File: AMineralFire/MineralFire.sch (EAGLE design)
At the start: 49 parts, among them IC1 LM358, Q1 20MHz, T1 200mA/40V, U1 328P, U3 7805

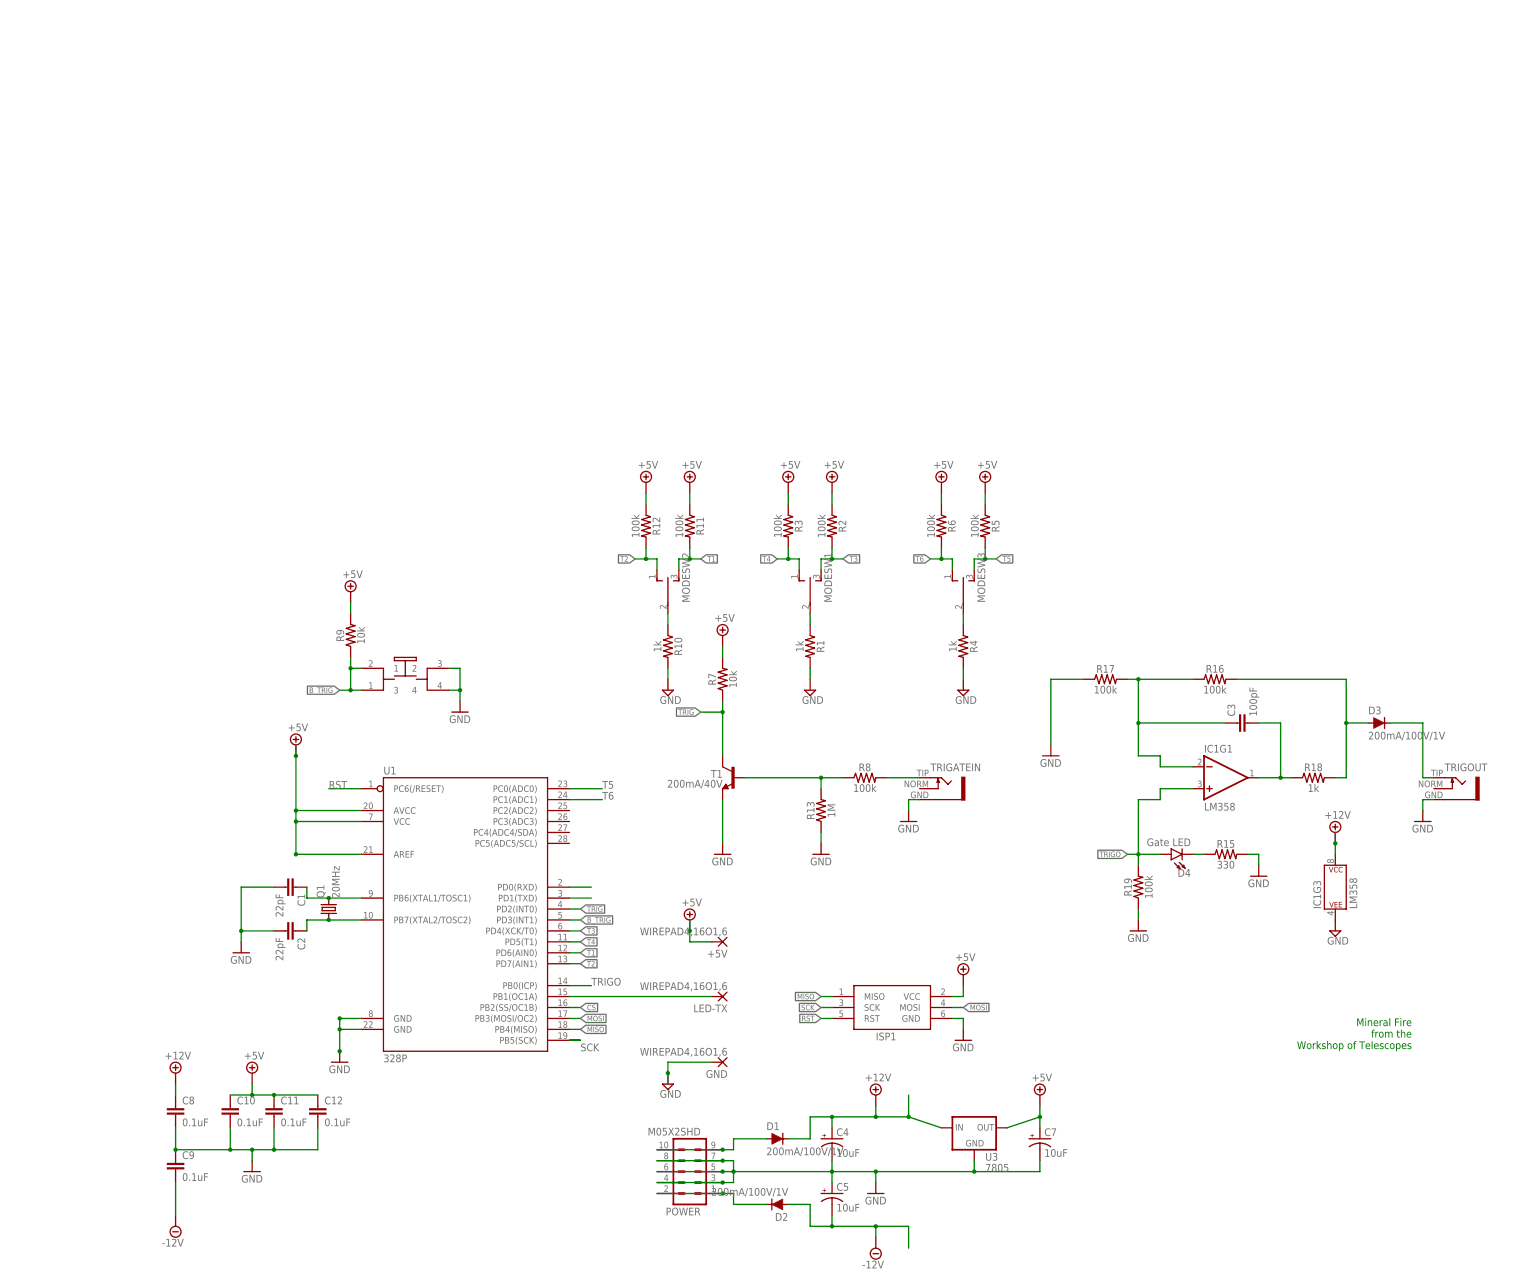
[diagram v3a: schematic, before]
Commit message: added LED in switch
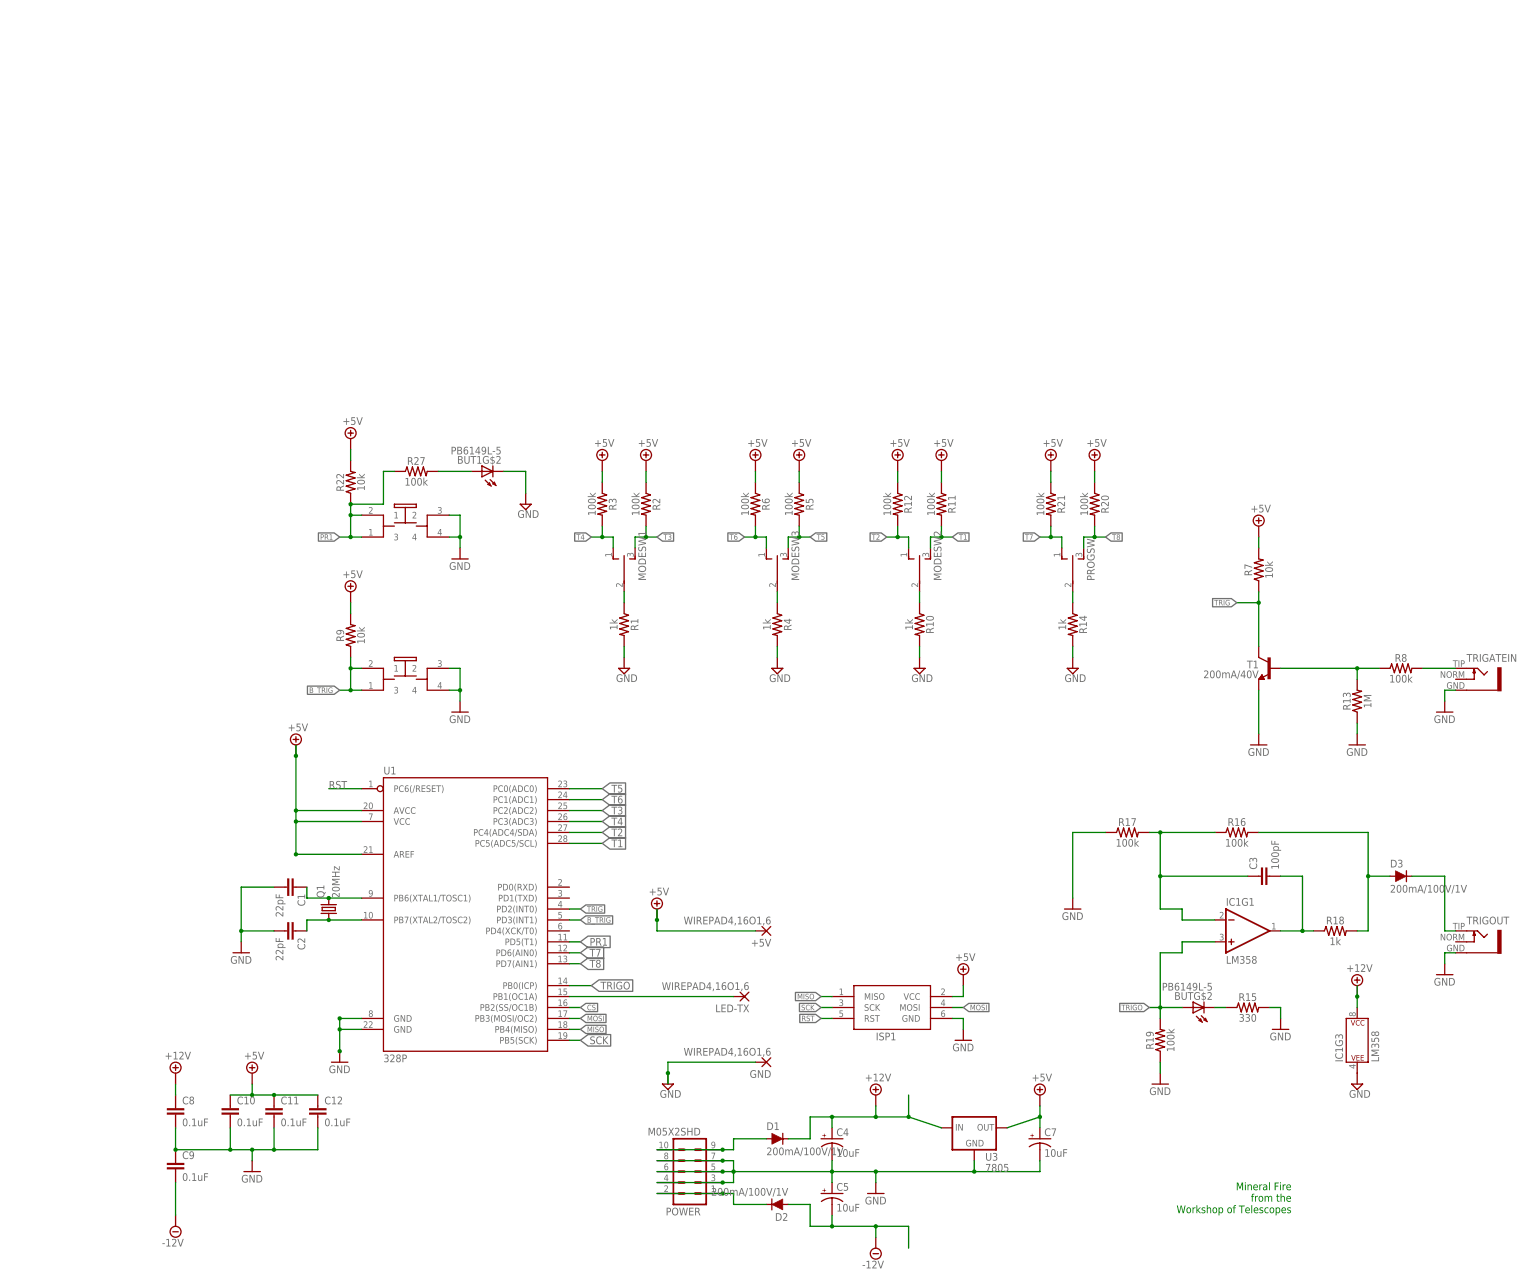
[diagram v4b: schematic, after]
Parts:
- removed D4: Gate LED, SparkFun-LED:LED3MM
- added BUT1: PB6149L-5, INSTRUO:PB6149L-5
- added PROGSW: TOGGLE_ON_OFF_ON, INSTRUO:TOGGLE_ON_OFF_ON
- added R14: 1k, SparkFun-Resistors:1KOHM-HORIZ-1/4W-5%
- added R20, R21, R27: 100k, SparkFun-Resistors:100KOHM-HORIZ-1/4W-5%
- added R22: 10k, SparkFun-Resistors:10KOHM-HORIZ-1/4W-1%
- renumbered START to BUT
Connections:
- new net N$16: BUT1G$2.A, R27.2
- new net N$6: PROGSW.P, R14.1
- new net PR1: BUT1G$1.1, BUT1G$1.3, R22.1, R27.1, U1.PD5(T1)
- new net T7: PROGSW.O, R21.2, U1.PD6(AIN0)
- new net T8: PROGSW.S, R20.2, U1.PD7(AIN1)
- net +5V: now also R20.1, R21.1, R22.2
- net GND: now also BUT1G$1.2, BUT1G$1.4, BUT1G$2.C, R14.2
- net N$31: now also BUTG$2.C; no longer D4.C
- net T1: now also U1.PC5(ADC5/SCL); no longer U1.PD6(AIN0)
- net T2: now also U1.PC4(ADC4/SDA); no longer U1.PD7(AIN1)
- net T3: now also U1.PC2(ADC2); no longer U1.PD4(XCK/T0)
- net T4: now also U1.PC3(ADC3); no longer U1.PD5(T1)
- net T5: no longer U1.PD0(RXD)
- net T6: no longer U1.PD1(TXD)
- net TRIGO: now also BUTG$2.A; no longer D4.A
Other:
- moved on the sheet: +5V, C3, D3, GND, IC1G1, IC1G3, LED-TX, MODESW1, MODESW2, MODESW3, R1, R10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

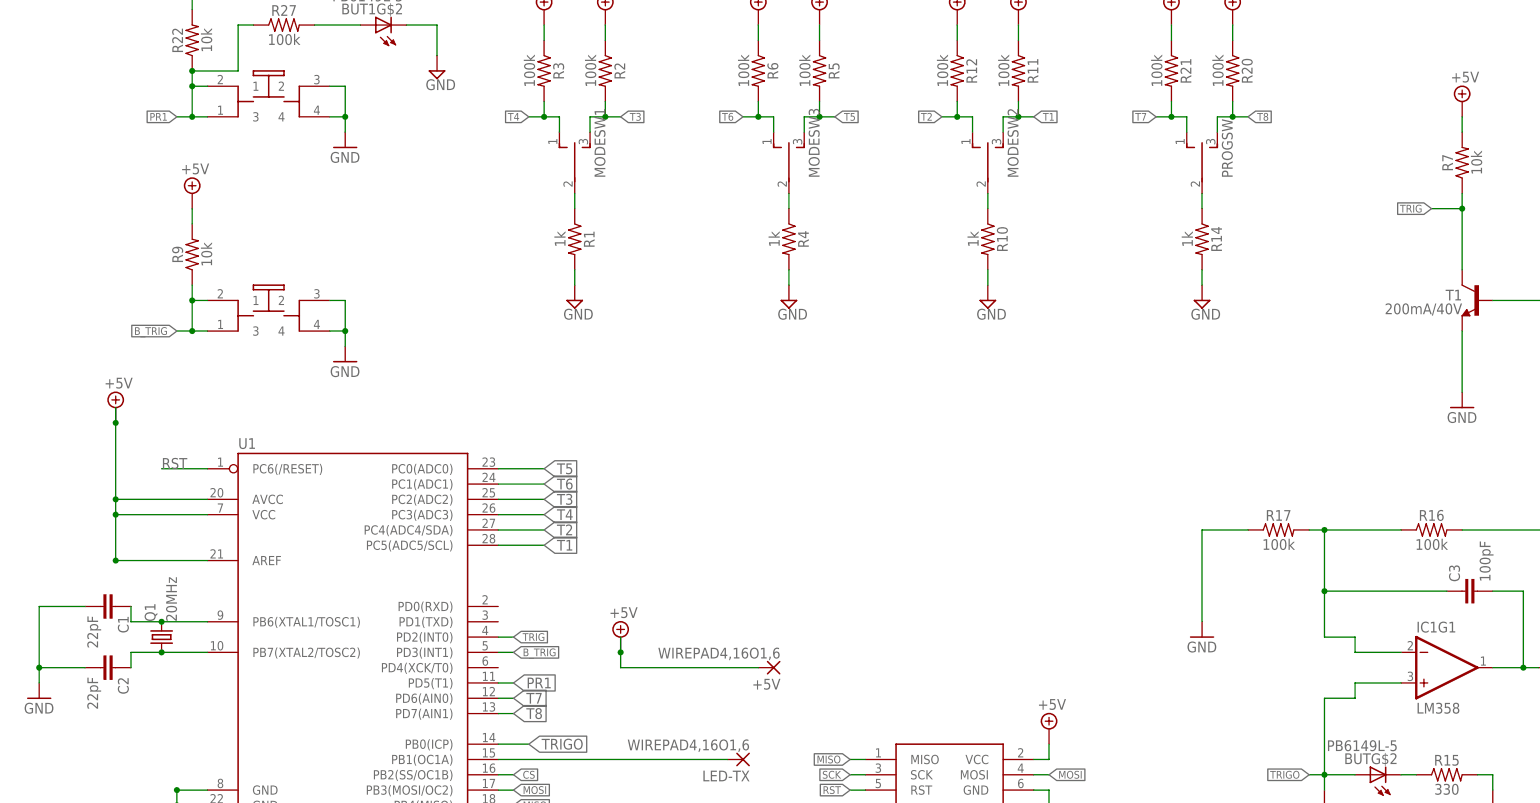
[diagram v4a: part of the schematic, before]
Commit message: Added AND gate on trigger
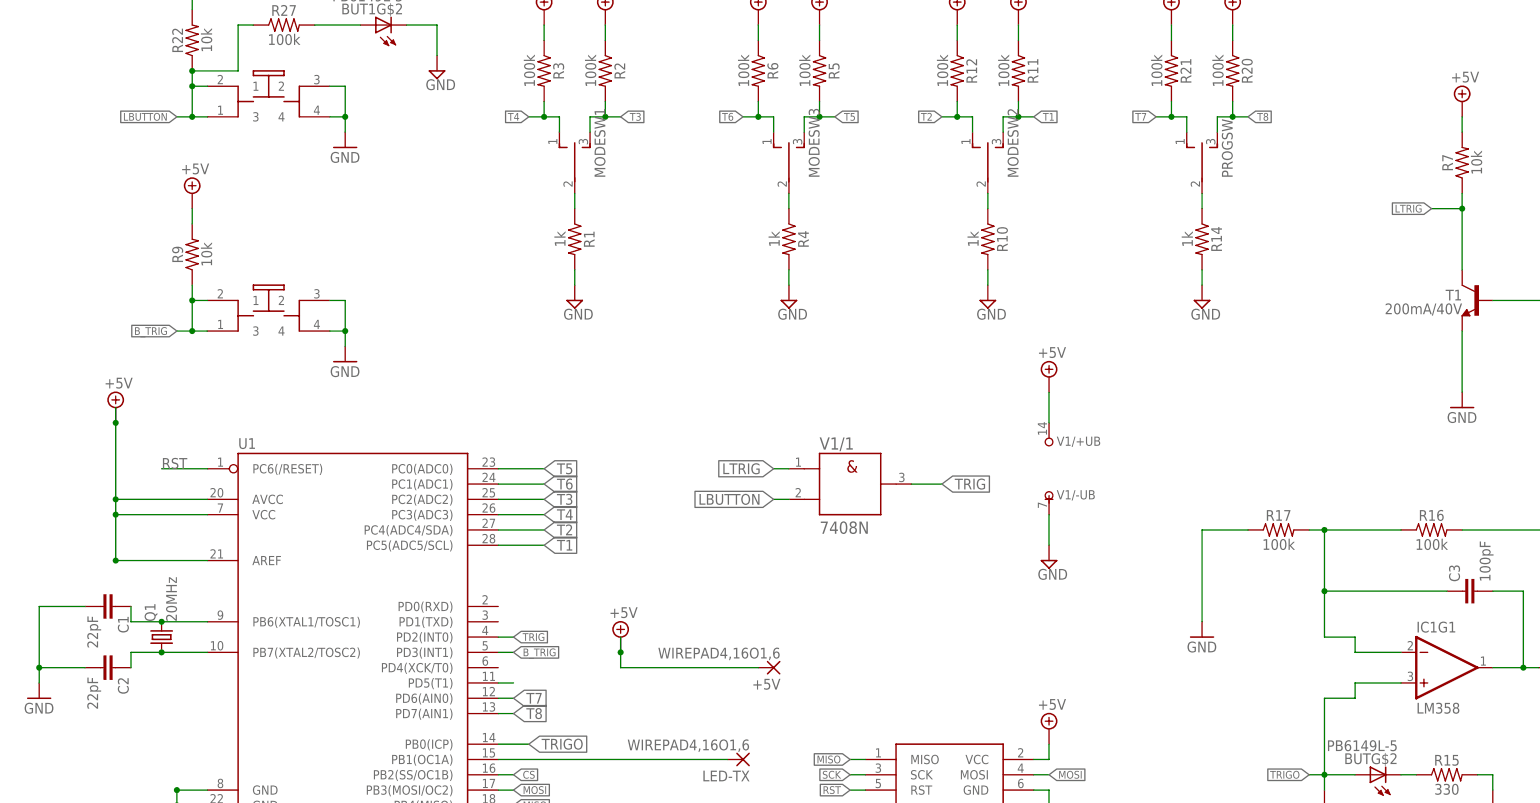
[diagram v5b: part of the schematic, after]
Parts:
- added V1: 7408N, 74ttl-din:7408N
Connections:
- new net LBUTTON: BUT1G$1.1, BUT1G$1.3, R22.1, R27.1, V1/1.B
- new net LTRIG: R7.1, T1.C, V1/1.A
- net +5V: now also V1/+UB.+UB
- net GND: now also V1/-UB.-UB
- net PR1: no longer BUT1G$1.1, BUT1G$1.3, R22.1, R27.1
- net TRIG: now also V1/1.Y; no longer R7.1, T1.C
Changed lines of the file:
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@@
 <part name="R27" library="SparkFun-Resistors" deviceset="100KOHM" device="-HORIZ-1/4W-5%" value="100k"/>
 <part name="SUPPLY30" library="supply2" deviceset="GND" device=""/>
+<part name="V1" library="74ttl-din" deviceset="74*08" device="N"/>
+<part name="SUPPLY28" library="supply2" deviceset="+5V" device=""/>
+<part name="SUPPLY29" library="supply2" deviceset="GND" device=""/>
 </parts>
 <sheets>
@@
 <instance part="R27" gate="G$1" x="76.2" y="142.24"/>
 <instance part="SUPPLY30" gate="GND" x="101.6" y="134.62"/>
+<instance part="V1" gate="/1" x="170.18" y="66.04"/>
+<instance part="V1" gate="/+UB" x="203.2" y="73.66"/>
+<instance part="SUPPLY28" gate="+5V" x="203.2" y="83.82"/>
+<instance part="V1" gate="/-UB" x="203.2" y="63.5"/>
+<instance part="SUPPLY29" gate="GND" x="203.2" y="53.34"/>
 </instances>
 <busses>
@@
 <pinref part="SUPPLY30" gate="GND" pin="GND"/>
 </segment>
+<segment>
+<pinref part="V1" gate="/-UB" pin="-UB"/>
+<wire x1="203.2" y1="60.96" x2="203.2" y2="55.88" width="0.1524" layer="91"/>
+<pinref part="SUPPLY29" gate="GND" pin="GND"/>
+</segment>
 </net>
 <net name="RST" class="0">
@@
 <pinref part="SUPPLY27" gate="+5V" pin="+5V"/>
 <wire x1="60.96" y1="147.32" x2="60.96" y2="144.78" width="0.1524" layer="91"/>
+</segment>
+<segment>
+<pinref part="V1" gate="/+UB" pin="+UB"/>
+<wire x1="203.2" y1="76.2" x2="203.2" y2="81.28" width="0.1524" layer="91"/>
+<pinref part="SUPPLY28" gate="+5V" pin="+5V"/>
 </segment>
 </net>
@@
 </segment>
 <segment>
-<pinref part="T1" gate="G$1" pin="C"/>
-<pinref part="R7" gate="G$1" pin="1"/>
-<wire x1="271.78" y1="114.3" x2="271.78" y2="111.76" width="0.1524" layer="91"/>
-<wire x1="271.78" y1="111.76" x2="271.78" y2="101.6" width="0.1524" layer="91"/>
-<wire x1="271.78" y1="111.76" x2="266.7" y2="111.76" width="0.1524" layer="91"/>
-<junction x="271.78" y="111.76"/>
-<label x="266.7" y="111.76" size="1.27" layer="95" rot="R180" xref="yes"/>
+<pinref part="V1" gate="/1" pin="Y"/>
+<wire x1="180.34" y1="66.04" x2="185.42" y2="66.04" width="0.1524" layer="91"/>
+<label x="185.42" y="66.04" size="1.778" layer="95" xref="yes"/>
 </segment>
 </net>
@@
 <pinref part="U1" gate="G$1" pin="PD5(T1)"/>
 <wire x1="111.76" y1="33.02" x2="114.3" y2="33.02" width="0.1524" layer="91"/>
-<label x="114.3" y="33.02" size="1.778" layer="95" xref="yes"/>
+</segment>
+</net>
+<net name="N$16" class="0">
+<segment>
+<pinref part="R27" gate="G$1" pin="2"/>
+<pinref part="BUT1" gate="G$2" pin="A"/>
+<wire x1="81.28" y1="142.24" x2="88.9" y2="142.24" width="0.1524" layer="91"/>
+</segment>
+</net>
+<net name="LTRIG" class="0">
+<segment>
+<pinref part="V1" gate="/1" pin="A"/>
+<wire x1="160.02" y1="68.58" x2="157.48" y2="68.58" width="0.1524" layer="91"/>
+<label x="157.48" y="68.58" size="1.778" layer="95" rot="R180" xref="yes"/>
+</segment>
+<segment>
+<pinref part="T1" gate="G$1" pin="C"/>
+<pinref part="R7" gate="G$1" pin="1"/>
+<wire x1="271.78" y1="114.3" x2="271.78" y2="111.76" width="0.1524" layer="91"/>
+<wire x1="271.78" y1="111.76" x2="271.78" y2="101.6" width="0.1524" layer="91"/>
+<wire x1="271.78" y1="111.76" x2="266.7" y2="111.76" width="0.1524" layer="91"/>
+<junction x="271.78" y="111.76"/>
+<label x="266.7" y="111.76" size="1.27" layer="95" rot="R180" xref="yes"/>
+</segment>
+</net>
+<net name="LBUTTON" class="0">
+<segment>
+<pinref part="V1" gate="/1" pin="B"/>
+<wire x1="160.02" y1="63.5" x2="157.48" y2="63.5" width="0.1524" layer="91"/>
+<label x="157.48" y="63.5" size="1.778" layer="95" rot="R180" xref="yes"/>
 </segment>
 <segment>
@@
 </segment>
 </net>
-<net name="N$16" class="0">
-<segment>
-<pinref part="R27" gate="G$1" pin="2"/>
-<pinref part="BUT1" gate="G$2" pin="A"/>
-<wire x1="81.28" y1="142.24" x2="88.9" y2="142.24" width="0.1524" layer="91"/>
-</segment>
-</net>
